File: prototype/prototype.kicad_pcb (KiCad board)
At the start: 4 copper layers, 78.7 x 63.5 mm, 47 parts, among them P1 CONN_25X2, P2 CONN_25X2, P3 VGACONN, U1 MC68SEC000, U2 FLASHROM_512K_16, U3 RAM_512K_16, U4 RAM_512K_16

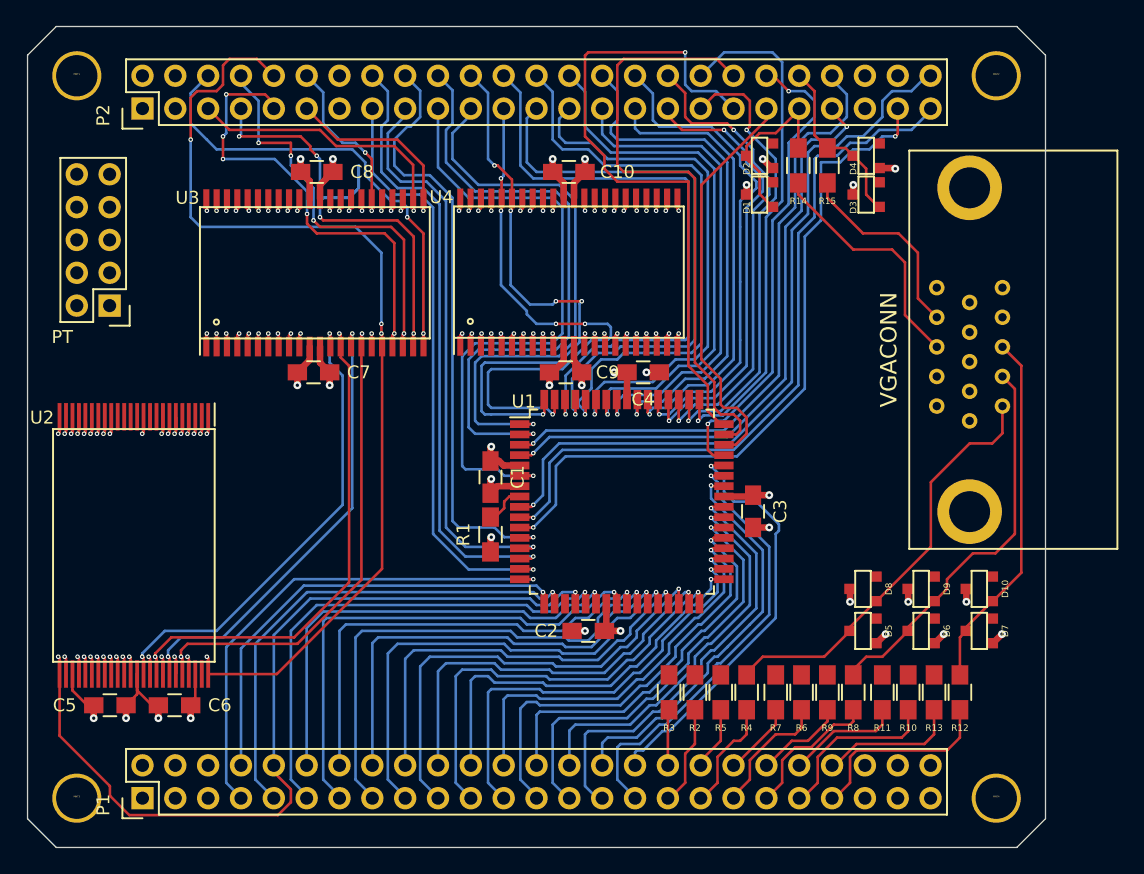
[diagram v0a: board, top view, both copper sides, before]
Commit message: Rip up all the traces and reorient the CPU at 45degrees.
Hopefully this will make for some tidier traces since we won't have to
route quite so far around the CPU with all of the bus traces.
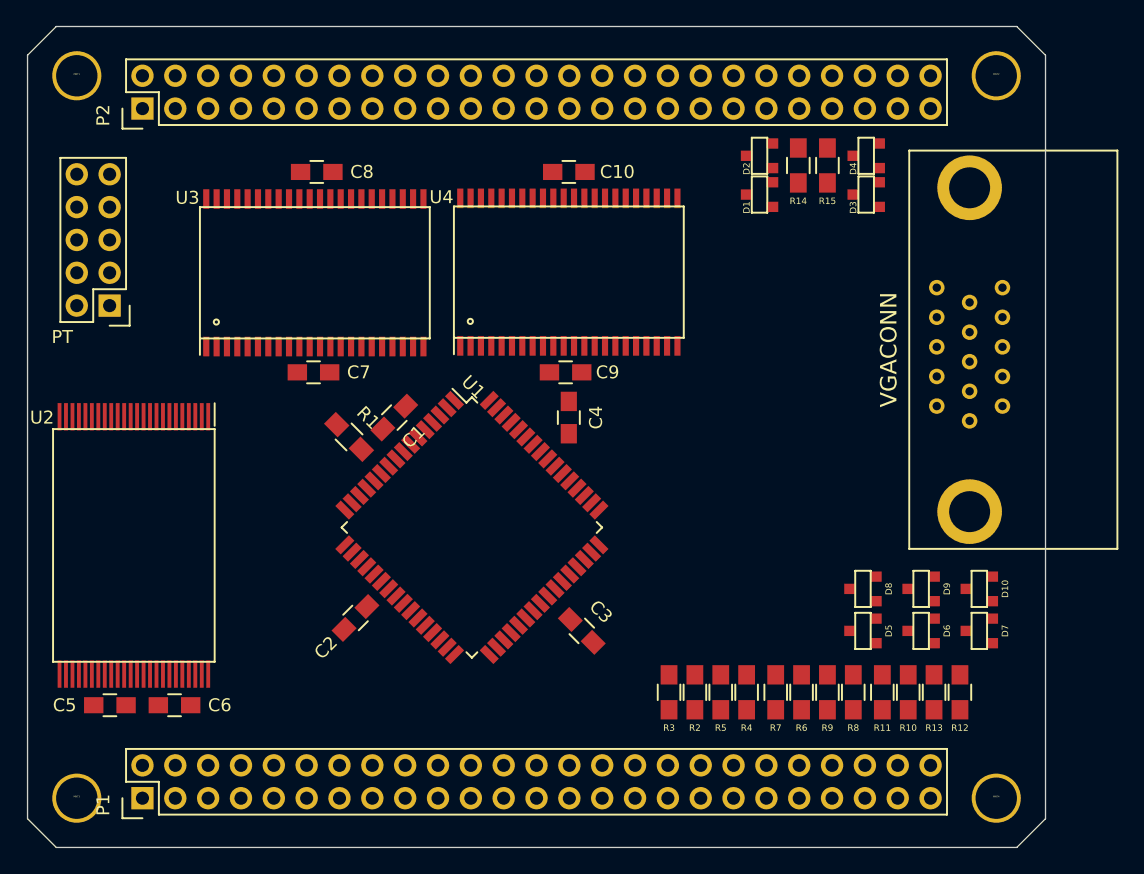
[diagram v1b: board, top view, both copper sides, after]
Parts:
- moved C2 18.0 mm to (137.8, 106.7), turned to 45 degrees
- moved C3 16.2 mm to (155.3, 107.7), turned to 315 degrees
- moved R1 13.3 mm to (137.3, 92.7), turned to 315 degrees
- moved U1 11.8 mm to (146.8, 99.7), turned to 315 degrees
- moved C1 8.75 mm to (140.8, 91.2), turned to 225 degrees
- moved C4 6.73 mm to (154.3, 91.2), turned to 270 degrees
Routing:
- net D5: track 80.0 -> 0.00 mm, vias 4 -> 0
- net PA17: track 77.9 -> 0.00 mm, vias 5 -> 0
- net D7: track 76.4 -> 0.00 mm, vias 4 -> 0
- net D4: track 75.9 -> 0.00 mm, vias 4 -> 0
- net D6: track 71.5 -> 0.00 mm, vias 4 -> 0
- net A1: track 69.0 -> 0.00 mm, vias 4 -> 0
- net ~HALT: track 57.6 -> 0.00 mm, vias 1 -> 0
- net ~RESET: track 56.3 -> 0.00 mm, vias 1 -> 0
- net ~AVEC: track 55.1 -> 0.00 mm, vias 2 -> 0
- net D12: track 54.5 -> 0.00 mm, vias 4 -> 0
- net D13: track 50.1 -> 0.00 mm, vias 3 -> 0
- net ~BG: track 49.1 -> 0.00 mm, vias 1 -> 0
- net D1: track 49.1 -> 0.00 mm, vias 4 -> 0
- net CLK: track 49.0 -> 0.00 mm, vias 1 -> 0
- net D0: track 48.6 -> 0.00 mm, vias 4 -> 0
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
